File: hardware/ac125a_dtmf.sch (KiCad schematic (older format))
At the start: 8 parts, among them J1 112-050-113R001

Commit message: Update schematic for Issue 2.
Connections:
- net at F1.1, J1.7: now also J1.MH1, J1.MH2
- no-connect marks 25 -> 30
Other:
- note added: "2"
- note added: "2020-05-24"
- note removed: "1"
- note removed: "2020-05-17"
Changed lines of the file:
@@
 F18 "ACT125A_PE1" I R 8150 4750 50
 F19 "ACT125A_C1" I R 8150 4850 50
+F20 "AC125A_B0" I L 6900 4150 50
 $EndSheet
 Text Label 5400 3550 2    50   ~ 0
@@
 Text Label 5400 3650 2    50   ~ 0
 AC125A_ST0
-Text Label 5400 3750 2    50   ~ 0
+Text Label 5500 3750 2    50   ~ 0
 AC125A_PA0
 Wire Wire Line
 	4900 3750 5500 3750
-Text Label 5400 3850 2    50   ~ 0
+Text Label 5500 3850 2    50   ~ 0
 AC125A_PC0
 Wire Wire Line
 	4900 3850 5500 3850
-Text Label 5400 3950 2    50   ~ 0
+Text Label 5500 3950 2    50   ~ 0
 AC125A_PE0
 Wire Wire Line
@@
 Text Label 6150 4150 2    50   ~ 0
 AC125A_B0
-Text Label 5400 4350 2    50   ~ 0
+Text Label 5500 4350 2    50   ~ 0
 AC125A_T1
-Text Label 5400 4450 2    50   ~ 0
+Text Label 5500 4450 2    50   ~ 0
 AC125A_ST1
-Text Label 5400 4550 2    50   ~ 0
+Text Label 5500 4550 2    50   ~ 0
 AC125A_PA1
 Wire Wire Line
 	4900 4550 5500 4550
-Text Label 5400 4650 2    50   ~ 0
+Text Label 5500 4650 2    50   ~ 0
 AC125A_PC1
 Wire Wire Line
 	4900 4650 5500 4650
-Text Label 5400 4750 2    50   ~ 0
+Text Label 5500 4750 2    50   ~ 0
 AC125A_PE1
 Wire Wire Line
@@
 Wire Wire Line
 	4900 4950 5500 4950
-Text Label 5450 4950 2    50   ~ 0
+Text Label 5500 4950 2    50   ~ 0
 AC125A_B1
 Wire Wire Line
@@
 Text Label 5450 5350 2    50   ~ 0
 AC125A_B2
-Text GLabel 8900 3650 2    50   Output ~ 0
-AC125A_PB0
 Wire Wire Line
 	8150 3650 8900 3650
-Text GLabel 8900 3550 2    50   Output ~ 0
-AC125A_PA0
 Wire Wire Line
 	8150 3550 8900 3550
-Text GLabel 8900 3850 2    50   Output ~ 0
-AC125A_PD0
 Wire Wire Line
 	8150 3850 8900 3850
-Text GLabel 8900 3750 2    50   Output ~ 0
-AC125A_PC0
 Wire Wire Line
 	8150 3750 8900 3750
-Text GLabel 8900 4050 2    50   Output ~ 0
-AC125A_C0
 Wire Wire Line
 	8150 4050 8900 4050
-Text GLabel 8900 3950 2    50   Output ~ 0
-AC125A_PE0
 Wire Wire Line
 	8150 3950 8900 3950
-Text GLabel 8900 4450 2    50   Output ~ 0
-AC125A_PB1
 Wire Wire Line
 	8150 4450 8900 4450
-Text GLabel 8900 4350 2    50   Output ~ 0
-AC125A_PA1
 Wire Wire Line
 	8150 4350 8900 4350
-Text GLabel 8900 4650 2    50   Output ~ 0
-AC125A_PD1
 Wire Wire Line
 	8150 4650 8900 4650
-Text GLabel 8900 4550 2    50   Output ~ 0
-AC125A_PC1
 Wire Wire Line
 	8150 4550 8900 4550
-Text GLabel 8900 4850 2    50   Output ~ 0
-AC125A_C1
 Wire Wire Line
 	8150 4850 8900 4850
-Text GLabel 8900 4750 2    50   Output ~ 0
-AC125A_PE1
 Wire Wire Line
 	8150 4750 8900 4750
-Text GLabel 5500 3850 2    50   Output ~ 0
-AC125A_PC0
-Text GLabel 5500 3750 2    50   Output ~ 0
-AC125A_PA0
-Text GLabel 5500 3950 2    50   Output ~ 0
-AC125A_PE0
-Text GLabel 6200 4150 2    50   Input ~ 0
-AC125A_B0
-Text GLabel 5500 4650 2    50   Output ~ 0
-AC125A_PC1
-Text GLabel 5500 4550 2    50   Output ~ 0
-AC125A_PA1
-Text GLabel 5500 4750 2    50   Output ~ 0
-AC125A_PE1
-Text GLabel 5500 4950 2    50   Input ~ 0
-AC125A_B1
-Text GLabel 5500 5350 2    50   Input ~ 0
-AC125A_B2
 $Comp
 L Device:CP1 C17
@@
 Text Label 2100 1550 2    50   ~ 0
 AC125A_G0
-Text GLabel 3300 5350 0    50   Input ~ 0
+Text Label 3300 5350 2    50   ~ 0
 AC125A_G2
-Text GLabel 3300 4950 0    50   Input ~ 0
+Wire Wire Line
+	3300 3550 3300 2600
+Text Label 3300 4950 2    50   ~ 0
 AC125A_G1
-Text GLabel 3300 4750 0    50   Output ~ 0
+Wire Wire Line
+	3900 4950 3300 4950
+Wire Wire Line
+	3300 4750 3900 4750
+Text Label 3300 4750 2    50   ~ 0
 AC125A_C1
-Text GLabel 3300 4650 0    50   Output ~ 0
+Wire Wire Line
+	3300 4650 3900 4650
+Text Label 3300 4650 2    50   ~ 0
 AC125A_PD1
-Text GLabel 3300 4550 0    50   Output ~ 0
+Wire Wire Line
+	3300 4550 3900 4550
+Text Label 3300 4550 2    50   ~ 0
 AC125A_PB1
-Text GLabel 3300 4350 0    50   Input ~ 0
+Text Label 3300 4350 2    50   ~ 0
 AC125A_R1
-Text GLabel 1550 4150 0    50   Input ~ 0
+Wire Wire Line
+	3300 4350 3900 4350
+Text Label 2800 4150 2    50   ~ 0
 AC125A_G0
-Text GLabel 3300 3950 0    50   Output ~ 0
+Wire Wire Line
+	3300 3950 3900 3950
+Text Label 3300 3950 2    50   ~ 0
 AC125A_C0
-Text GLabel 3300 3850 0    50   Output ~ 0
+Wire Wire Line
+	3300 3850 3900 3850
+Text Label 3300 3850 2    50   ~ 0
 AC125A_PD0
-Text GLabel 3300 3750 0    50   Output ~ 0
-AC125A_PB0
-Text Label 3850 5350 2    50   ~ 0
-AC125A_G2
-Wire Wire Line
-	3300 5350 3900 5350
-Wire Wire Line
-	3300 3550 3300 2600
-Text Label 3750 4950 2    50   ~ 0
-AC125A_G1
-Wire Wire Line
-	3900 4950 3300 4950
-Wire Wire Line
-	3300 4750 3900 4750
-Text Label 3800 4750 2    50   ~ 0
-AC125A_C1
-Wire Wire Line
-	3300 4650 3900 4650
-Text Label 3800 4650 2    50   ~ 0
-AC125A_PD1
-Wire Wire Line
-	3300 4550 3900 4550
-Text Label 3800 4550 2    50   ~ 0
-AC125A_PB1
-Text Label 3800 4350 2    50   ~ 0
-AC125A_R1
-Wire Wire Line
-	3300 4350 3900 4350
-Text Label 2200 4150 2    50   ~ 0
-AC125A_G0
-Wire Wire Line
-	3300 3950 3900 3950
-Text Label 3800 3950 2    50   ~ 0
-AC125A_C0
-Wire Wire Line
-	3300 3850 3900 3850
-Text Label 3800 3850 2    50   ~ 0
-AC125A_PD0
 Wire Wire Line
 	3300 3750 3900 3750
-Text Label 3800 3750 2    50   ~ 0
+Text Label 3300 3750 2    50   ~ 0
 AC125A_PB0
 Text Label 3800 3550 2    50   ~ 0
@@
 $EndComp
 Wire Wire Line
-	1550 4150 2300 4150
-Wire Wire Line
 	2300 1550 2300 4150
 Wire Wire Line
-	3900 4150 3350 4150
+	3900 4150 3700 4150
 Wire Wire Line
 	3050 4150 2300 4150
-Connection ~ 2300 4150
 $Comp
 L Device:Fuse F2
@@
 $EndComp
 Wire Wire Line
-	5550 4150 6200 4150
-Wire Wire Line
 	5250 4150 4900 4150
 Text Notes 7500 7500 0    50   ~ 0
 OKI AC125A DTMF Converter - PBX Interface and Power Supply
 Text Notes 8200 7650 0    50   ~ 0
-2020-05-17
+2020-05-24
 Text Notes 10600 7650 0    50   ~ 0
-1
+2
 Text Notes 6250 1700 0    50   ~ 0
 Power LED
@@
 U 1 1 5ECC0265
 P 4400 6250
-F 0 "J1" V 7581 6250 50  0000 C CNN
-F 1 "112-050-113R001" V 7490 6250 50  0000 C CNN
+F 0 "J1" V 7700 6250 50  0000 C CNN
+F 1 "112-050-113R001" V 7600 6250 50  0000 C CNN
 F 2 "112050113R001" H 7250 6550 50  0001 L CNN
 F 3 "https://componentsearchengine.com/Datasheets/1/112-050-113R001.pdf" H 7250 6450 50  0001 L CNN
@@
 	0    -1   -1   0
 $EndComp
+Wire Wire Line
+	4400 6250 4400 6350
+Wire Wire Line
+	4400 6350 3700 6350
+Wire Wire Line
+	3700 3150 4400 3150
+Wire Wire Line
+	4400 3150 4400 3250
+Wire Wire Line
+	5550 4150 6900 4150
+Wire Wire Line
+	3700 3150 3700 4150
+Connection ~ 3700 4150
+Wire Wire Line
+	3700 4150 3350 4150
+Wire Wire Line
+	3300 5350 3900 5350
+Wire Wire Line
+	3700 6350 3700 4150
+NoConn ~ 5500 5150
+Text Label 8900 4050 2    50   ~ 0
+AC125A_C0
+Text Label 8900 3750 2    50   ~ 0
+AC125A_PC0
+Text Label 8900 3550 2    50   ~ 0
+AC125A_PA0
+Text Label 8900 3650 2    50   ~ 0
+AC125A_PB0
+Text Label 8900 3850 2    50   ~ 0
+AC125A_PD0
+Text Label 8900 3950 2    50   ~ 0
+AC125A_PE0
+NoConn ~ 5500 4950
+NoConn ~ 3300 4950
+NoConn ~ 3300 5350
+NoConn ~ 5500 5350
+Text Label 8900 4450 2    50   ~ 0
+AC125A_PB1
+Text Label 8900 4850 2    50   ~ 0
+AC125A_C1
+Text Label 8900 4650 2    50   ~ 0
+AC125A_PD1
+Text Label 8900 4350 2    50   ~ 0
+AC125A_PA1
+Text Label 8900 4550 2    50   ~ 0
+AC125A_PC1
+Text Label 8900 4750 2    50   ~ 0
+AC125A_PE1
 $EndSCHEMATC

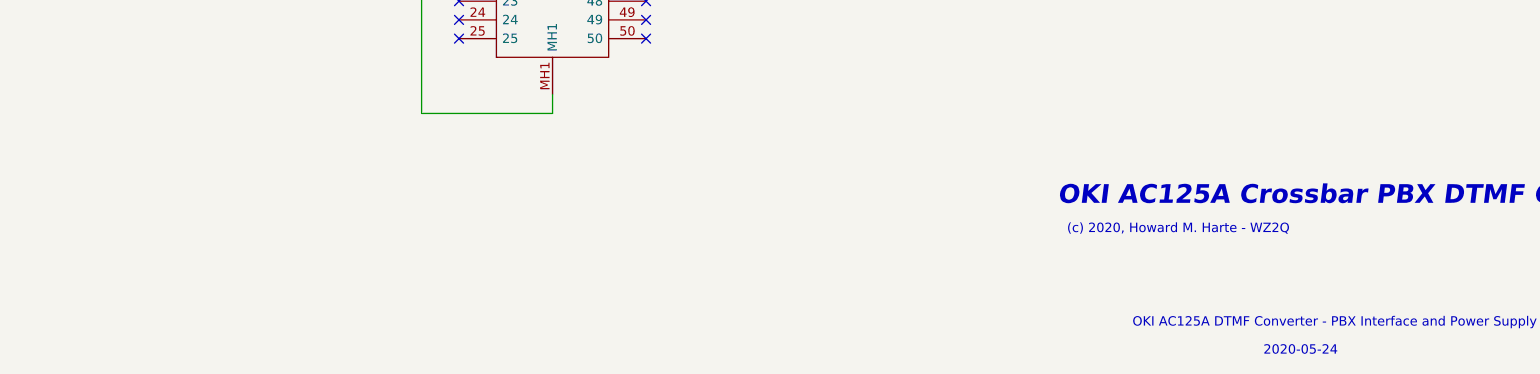
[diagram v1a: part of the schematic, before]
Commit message: Final schematic and PCB layout for Issue 2.
Corrected errors in Issue 1 and fabbed out the PCB.
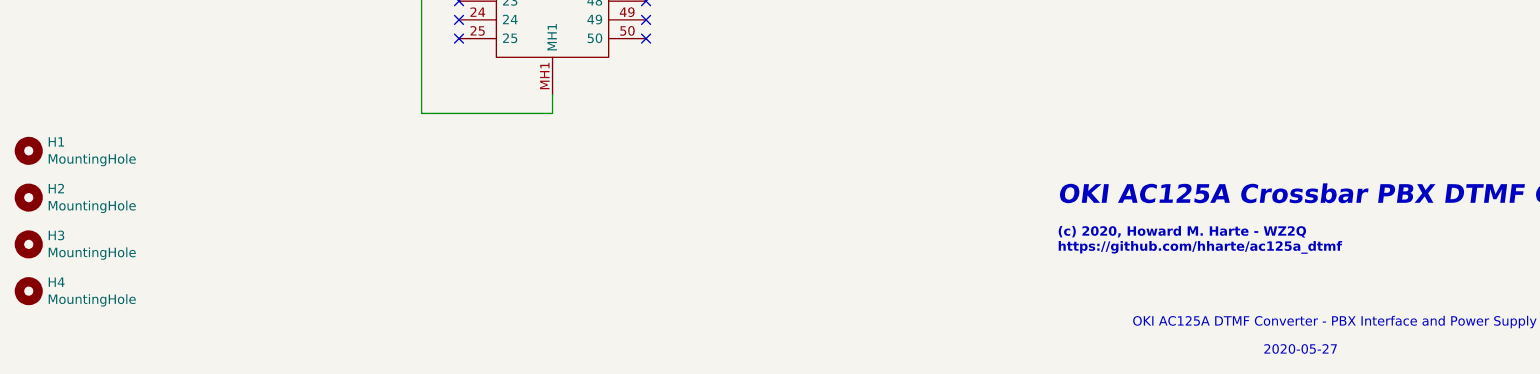
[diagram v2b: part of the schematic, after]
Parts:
- added H1, H2, H3, H4: MountingHole, MountingHole:MountingHole_3.7mm_Pad, symbol Mechanical:MountingHole
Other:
- note added: "(c) 2020, Howard M. Harte - WZ2Q\nhttps://github.com/hharte/ac125a_dtmf"
- note added: "2020-05-27"
- note removed: "(c) 2020, Howard M. Harte - WZ2Q"
- note removed: "2020-05-24"
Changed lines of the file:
@@
 OKI AC125A DTMF Converter - PBX Interface and Power Supply
 Text Notes 8200 7650 0    50   ~ 0
-2020-05-24
+2020-05-27
 Text Notes 10600 7650 0    50   ~ 0
 2
@@
 Text Notes 7100 6850 0    100  Italic 20
 OKI AC125A Crossbar PBX DTMF Converter
-Text Notes 7150 7000 0    50   ~ 0
-(c) 2020, Howard M. Harte - WZ2Q
+Text Notes 7100 7100 0    50   ~ 10
+(c) 2020, Howard M. Harte - WZ2Q\nhttps://github.com/hharte/ac125a_dtmf
 NoConn ~ 3900 3650
 NoConn ~ 3900 4050
@@
 Text Label 8900 4750 2    50   ~ 0
 AC125A_PE1
+$Comp
+L Mechanical:MountingHole H1
+U 1 1 5F4E24D8
+P 1600 6550
+F 0 "H1" H 1700 6596 50  0000 L CNN
+F 1 "MountingHole" H 1700 6505 50  0000 L CNN
+F 2 "MountingHole:MountingHole_3.7mm_Pad" H 1600 6550 50  0001 C CNN
+F 3 "~" H 1600 6550 50  0001 C CNN
+	1    1600 6550
+	1    0    0    -1
+$EndComp
+$Comp
+L Mechanical:MountingHole H2
+U 1 1 5F4E2831
+P 1600 6800
+F 0 "H2" H 1700 6846 50  0000 L CNN
+F 1 "MountingHole" H 1700 6755 50  0000 L CNN
+F 2 "MountingHole:MountingHole_3.7mm_Pad" H 1600 6800 50  0001 C CNN
+F 3 "~" H 1600 6800 50  0001 C CNN
+	1    1600 6800
+	1    0    0    -1
+$EndComp
+$Comp
+L Mechanical:MountingHole H3
+U 1 1 5F4E613B
+P 1600 7050
+F 0 "H3" H 1700 7096 50  0000 L CNN
+F 1 "MountingHole" H 1700 7005 50  0000 L CNN
+F 2 "MountingHole:MountingHole_3.7mm_Pad" H 1600 7050 50  0001 C CNN
+F 3 "~" H 1600 7050 50  0001 C CNN
+	1    1600 7050
+	1    0    0    -1
+$EndComp
+$Comp
+L Mechanical:MountingHole H4
+U 1 1 5F4E6141
+P 1600 7300
+F 0 "H4" H 1700 7346 50  0000 L CNN
+F 1 "MountingHole" H 1700 7255 50  0000 L CNN
+F 2 "MountingHole:MountingHole_3.7mm_Pad" H 1600 7300 50  0001 C CNN
+F 3 "~" H 1600 7300 50  0001 C CNN
+	1    1600 7300
+	1    0    0    -1
+$EndComp
 $EndSCHEMATC
